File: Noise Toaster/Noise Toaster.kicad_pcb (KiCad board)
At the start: 2 copper layers, 163.1 x 101.3 mm, 133 parts, among them J1 AudioJack3_SwitchTR, Q1 2N3904, Q10 2N5457, Q2 2N3904, Q3 2N5457, Q4 2N5457, Q5 2N3904, Q6 2N3904, Q7 2N3904, Q8 2N5457, Q9 2N3906, U1 LM324, U2 LM324, U3 LM386

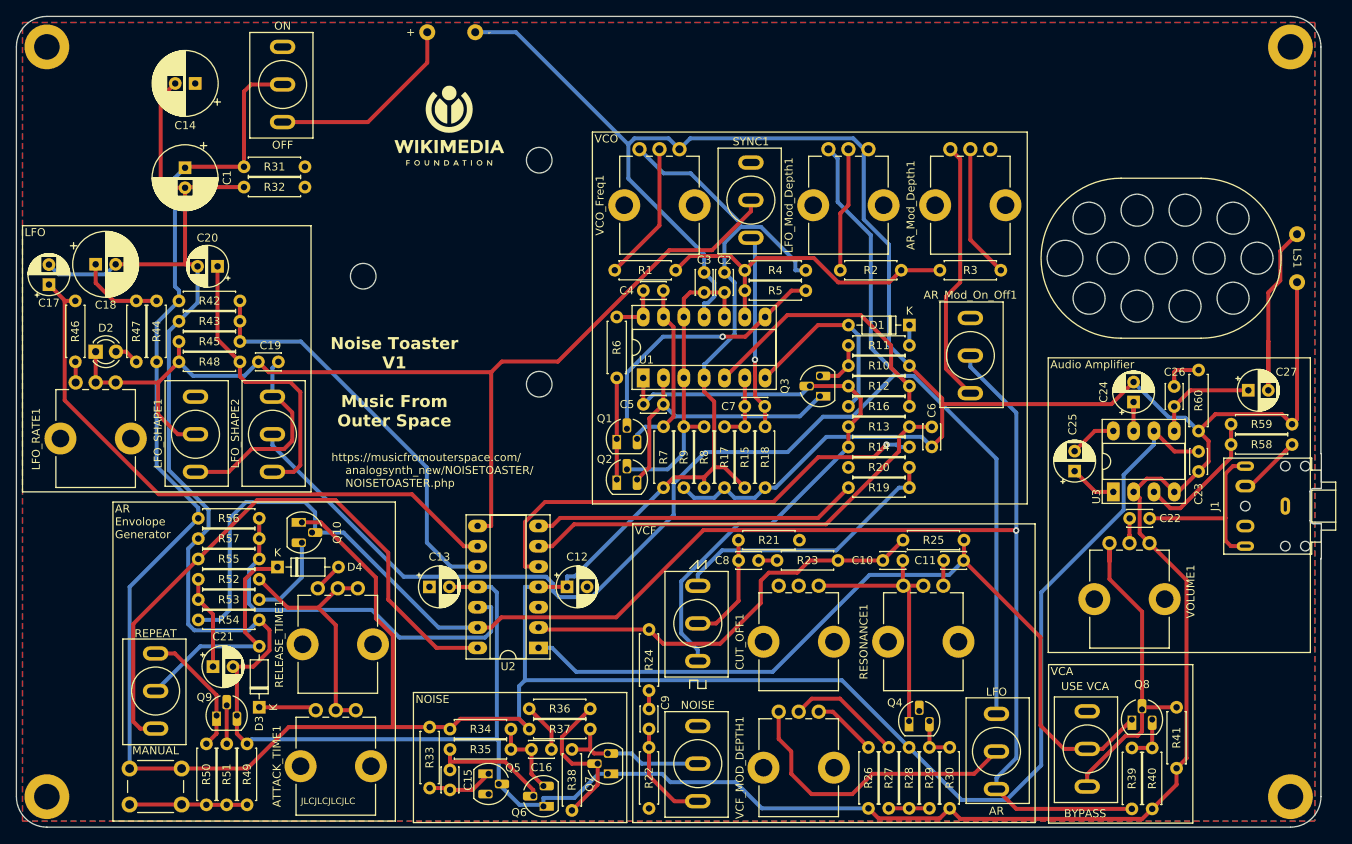
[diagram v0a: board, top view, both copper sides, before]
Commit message: Noise Toaster - fixes after first board
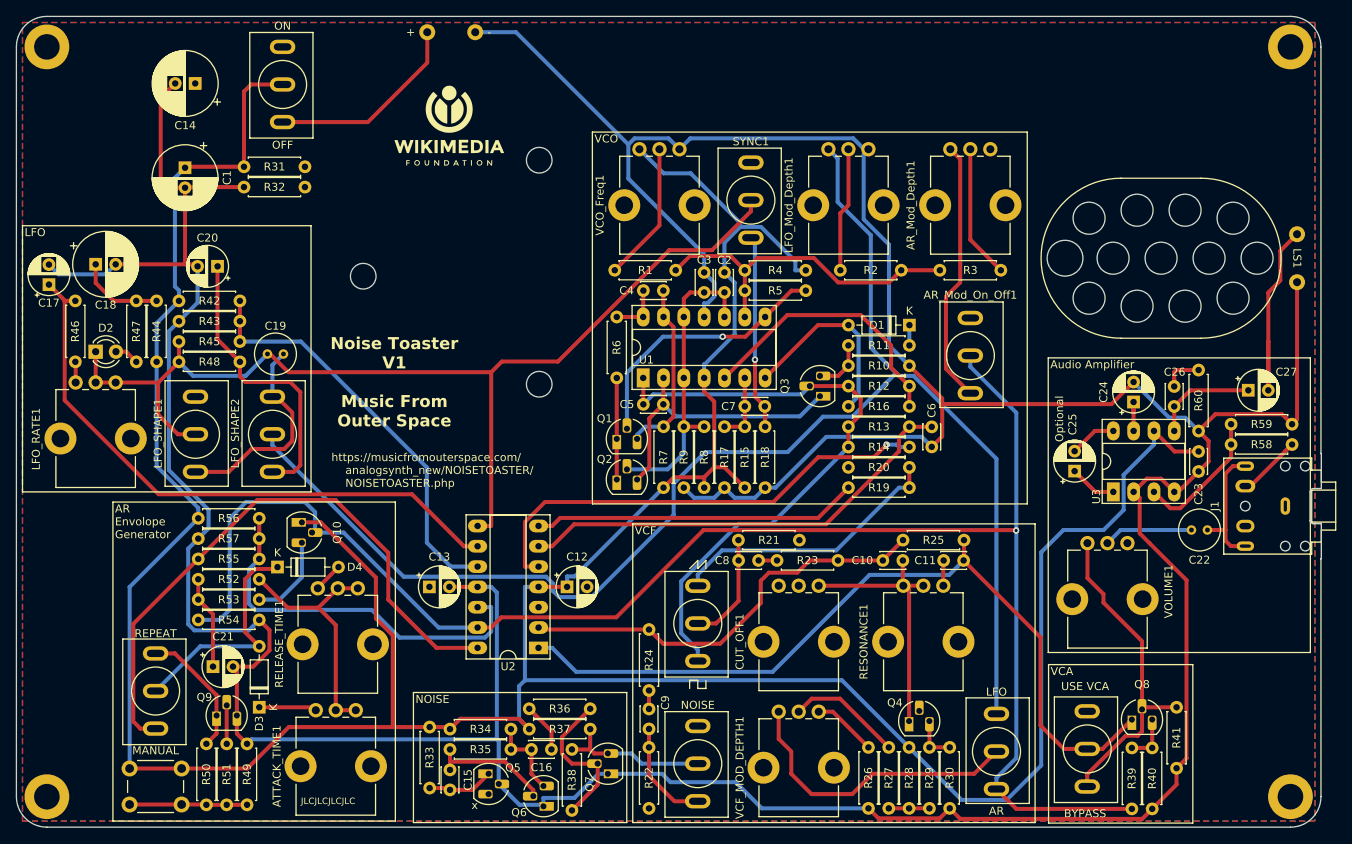
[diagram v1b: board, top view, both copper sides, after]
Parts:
- C19, C22: value 100nF -> 1uF; footprint Capacitor_THT:C_Disc_D3.0mm_W2.0mm_P2.50mm -> Capacitor_THT:C_Radial_D5.0mm_H7.0mm_P2.00mm
- C21: value 1uF -> 4.7uF
- R36: value 10K -> 100K
- R4: value 75K -> 270K
- R5: value 75K -> 2K
- R50: value 10K -> 200R
- moved C22 7.37 mm to (204.0, 115.0)
- moved VOLUME1 2.76 mm to (191.5, 123.6)
- moved C19 1.17 mm to (88.5, 93.0)
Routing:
- net Net-(C22-Pad1): track 24.5 -> 17.2 mm
- net Net-(C22-Pad2): track 4.12 -> 11.2 mm
- net BP: track 433.4 -> 436.3 mm
- net Net-(LFO_SHAPE1-C): track 25.2 -> 26.5 mm
- net AUDIO_OUT: track 42.7 -> 41.6 mm
- net SYNC: track 131.7 -> 132.5 mm
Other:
- board text added: "Optional"
- board text added: "x"

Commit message: misc
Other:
- board text added: "fast"
- board text added: "slow"
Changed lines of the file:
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@@
+    (effects (font (size 1 1) (thickness 0.15)) (justify left bottom))
+  )
+  (gr_text "fast" (at 98.806 138.176) (layer "F.SilkS")
     (effects (font (size 1 1) (thickness 0.15)) (justify left bottom))
   )
@@
     (effects (font (size 1 1) (thickness 0.15)) (justify left top))
   )
-  (gr_text "AR" (at 177.628 149.54) (layer "F.SilkS")
-    (effects (font (size 1 1) (thickness 0.15)) (justify top))
+  (gr_text "AR" (at 177.778 135.89) (layer "F.SilkS")
+    (effects (font (size 1 1) (thickness 0.15)) (justify bottom))
   )
   (gr_text "LFO" (at 56.134 77.216) (layer "F.SilkS")
@@
     (effects (font (size 1 1) (thickness 0.15)) (justify left top))
   )
+  (gr_text "slow" (at 91.44 122.936) (layer "F.SilkS")
+    (effects (font (size 1 1) (thickness 0.15)) (justify right bottom))
+  )
+  (gr_text "fast" (at 99.06 122.936) (layer "F.SilkS")
+    (effects (font (size 1 1) (thickness 0.15)) (justify left bottom))
+  )
   (gr_text "OFF" (at 88.392 66.294) (layer "F.SilkS")
     (effects (font (size 1 1) (thickness 0.15)) (justify top))
   )
-  (gr_text "BYPASS" (at 188.71 149.86) (layer "F.SilkS")
-    (effects (font (size 1 1) (thickness 0.15)) (justify top))
+  (gr_text "BYPASS" (at 188.976 135.636) (layer "F.SilkS")
+    (effects (font (size 1 1) (thickness 0.15)) (justify bottom))
   )
   (gr_text "REPEAT" (at 72.517 128.524) (layer "F.SilkS")
@@
     (effects (font (size 1 1) (thickness 0.15)) (justify left top))
   )
-  (gr_text "LFO" (at 177.628 135.824) (layer "F.SilkS")
-    (effects (font (size 1 1) (thickness 0.15)) (justify bottom))
+  (gr_text "LFO" (at 177.546 149.352) (layer "F.SilkS")
+    (effects (font (size 1 1) (thickness 0.15)) (justify top))
   )
-  (gr_text "USE VCA" (at 188.71 135.128) (layer "F.SilkS")
-    (effects (font (size 1 1) (thickness 0.15)) (justify bottom))
+  (gr_text "USE VCA" (at 188.976 149.352) (layer "F.SilkS")
+    (effects (font (size 1 1) (thickness 0.15)) (justify top))
   )
   (gr_text "ON" (at 88.392 52.578) (layer "F.SilkS")
@@
     (effects (font (size 0.8 0.8) (thickness 0.15)) (justify left bottom))
   )
+  (gr_text "slow" (at 91.186 138.176) (layer "F.SilkS")
+    (effects (font (size 1 1) (thickness 0.15)) (justify right bottom))
+  )
   (gr_text_box "Data Platform Engineering\nOffsite - 2024\nWMF"
